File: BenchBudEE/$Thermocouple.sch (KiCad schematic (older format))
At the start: 23 parts, among them P2 CONN_3X2, P3 CONN_2, U4 OPA4170, U5 MCP3901, U6 LMT84

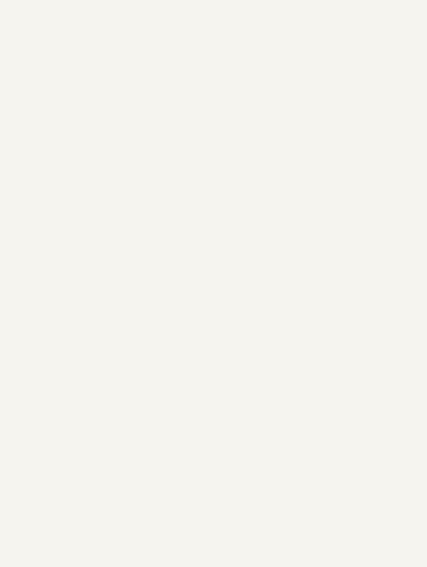
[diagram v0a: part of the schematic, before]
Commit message: Connectors added + associated + roughly placed.
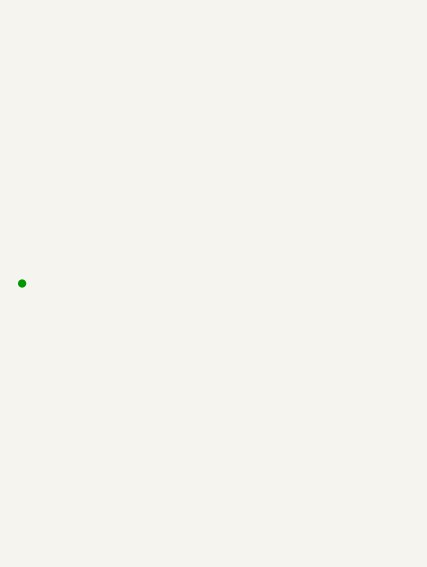
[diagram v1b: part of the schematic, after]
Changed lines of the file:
@@
 Wire Wire Line
 	5200 2800 5200 4000
+Connection ~ -5000 2900
 $EndSCHEMATC
